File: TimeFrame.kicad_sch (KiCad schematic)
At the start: 7 parts, among them J1 USB4105-GF-A

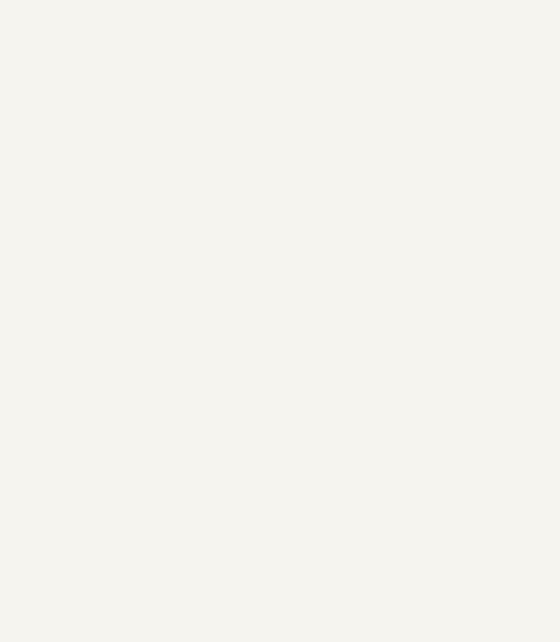
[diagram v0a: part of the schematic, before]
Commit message: Adding Encoders
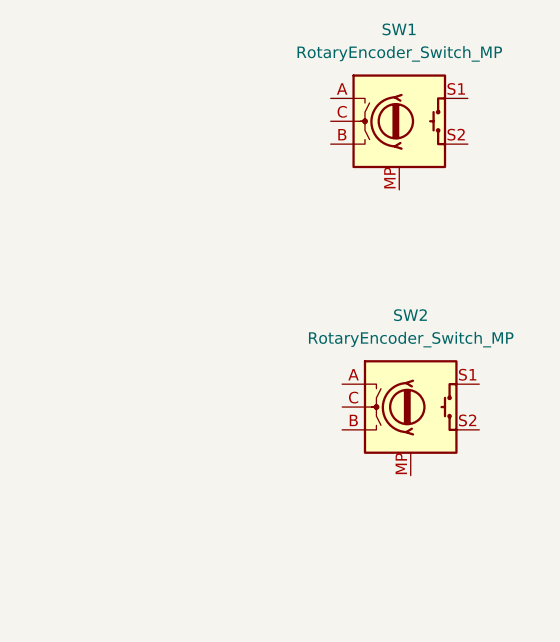
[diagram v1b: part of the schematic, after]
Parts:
- added SW1, SW2: RotaryEncoder_Switch_MP, AC-kicad-library:RotaryEncoder_Bourns_PEC11R-4220F-S0024_Vertical_H20mm_CircularMountingHoles, symbol AC-kicad-library:RotaryEncoder_Switch_PEC11R-4220F-S0024
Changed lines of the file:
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@@
+	)
+	(symbol
+		(lib_id "AC-kicad-library:RotaryEncoder_Switch_PEC11R-4220F-S0024")
+		(at 152.4 139.7 0)
+		(unit 1)
+		(exclude_from_sim no)
+		(in_bom yes)
+		(on_board yes)
+		(dnp no)
+		(fields_autoplaced yes)
+		(property "Reference" "SW2"
+			(at 152.4 129.54 0)
+			(effects
+				(font
+					(size 1.27 1.27)
+				)
+			)
+		)
+		(property "Value" "RotaryEncoder_Switch_MP"
+			(at 152.4 132.08 0)
+			(effects
+				(font
+					(size 1.27 1.27)
+				)
+			)
+		)
+		(property "Footprint" "AC-kicad-library:RotaryEncoder_Bourns_PEC11R-4220F-S0024_Vertical_H20mm_CircularMountingHoles"
+			(at 148.59 135.636 0)
+			(effects
+				(font
+					(size 1.27 1.27)
+				)
+				(hide yes)
+			)
+		)
+		(property "Datasheet" "https://www.lcsc.com/datasheet/lcsc_datasheet_2410010303_BOURNS-PEC11R-4220F-S0024_C143797.pdf"
+			(at 152.4 152.4 0)
+			(effects
+				(font
+					(size 1.27 1.27)
+				)
+				(hide yes)
+			)
+		)
+		(property "Description" "Rotary encoder, dual channel, incremental quadrate outputs, with switch and MP Pin"
+			(at 152.4 154.94 0)
+			(effects
+				(font
+					(size 1.27 1.27)
+				)
+				(hide yes)
+			)
+		)
+		(pin "S1"
+		)
+		(pin "B"
+		)
+		(pin "MP"
+		)
+		(pin "A"
+		)
+		(pin "S2"
+		)
+		(pin "C"
+		)
+		(instances
+			(project "TimeFrame"
+				(path "/e7c24600-e1d4-4e1e-8b2a-6e1d00e73a4d"
+					(reference "SW2")
+					(unit 1)
+				)
+			)
+		)
 	)
 	(symbol
@@
 					(unit 1)
 				)
+			)
+		)
+	)
+	(symbol
+		(lib_id "AC-kicad-library:RotaryEncoder_Switch_PEC11R-4220F-S0024")
+		(at 151.13 107.95 0)
+		(unit 1)
+		(exclude_from_sim no)
+		(in_bom yes)
+		(on_board yes)
+		(dnp no)
+		(fields_autoplaced yes)
+		(property "Reference" "SW1"
+			(at 151.13 97.79 0)
+			(effects
+				(font
+					(size 1.27 1.27)
+				)
+			)
+		)
+		(property "Value" "RotaryEncoder_Switch_MP"
+			(at 151.13 100.33 0)
+			(effects
+				(font
+					(size 1.27 1.27)
+				)
+			)
+		)
+		(property "Footprint" "AC-kicad-library:RotaryEncoder_Bourns_PEC11R-4220F-S0024_Vertical_H20mm_CircularMountingHoles"
+			(at 147.32 103.886 0)
+			(effects
+				(font
+					(size 1.27 1.27)
+				)
+				(hide yes)
+			)
+		)
+		(property "Datasheet" "https://www.lcsc.com/datasheet/lcsc_datasheet_2410010303_BOURNS-PEC11R-4220F-S0024_C143797.pdf"
+			(at 151.13 120.65 0)
+			(effects
+				(font
+					(size 1.27 1.27)
+				)
+				(hide yes)
+			)
+		)
+		(property "Description" "Rotary encoder, dual channel, incremental quadrate outputs, with switch and MP Pin"
+			(at 151.13 123.19 0)
+			(effects
+				(font
+					(size 1.27 1.27)
+				)
+				(hide yes)
+			)
+		)
+		(pin "S1"
+		)
+		(pin "B"
+		)
+		(pin "MP"
+		)
+		(pin "A"
+		)
+		(pin "S2"
+		)
+		(pin "C"
+		)
+		(instances
+			(project ""
+				(path "/e7c24600-e1d4-4e1e-8b2a-6e1d00e73a4d"
+					(reference "SW1")
+					(unit 1)
+				)
